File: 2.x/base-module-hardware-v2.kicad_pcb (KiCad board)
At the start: 4 copper layers, 100 x 99.7 mm, 271 parts, among them K1 CONN_3, P1 PINBALL-CONNECTOR, P2 PINBALL-CONNECTOR, P3 SOLENOID-CONNECTOR, P4 CONN_16, P5 CONN_16, P6 HE10-32, Q1 BC846, Q10 DMN6040SSD, Q11 BC846, Q12 BC846, Q13 DMP2240UDM, Q14 DMP2240UDM, Q15 BC846, Q16 BC846, Q17 BC846, Q18 BC846, Q19 DMN6040SSD, Q2 BC846, Q20 DMN6040SSD, Q21 BC846, Q22 BC846, Q23 BC846, Q24 BC846, Q25 BC846, Q26 BC846, Q27 BC846, Q28 BC846, Q29 BSS138, Q3 DMN6040SSD, Q30 FDD5614P, Q31 BC846, Q32 BSS138, Q4 DMN6040SSD, Q5 BC846, Q6 BC846, Q7 BC846, Q8 BC846, Q9 DMN6040SSD, U1 74LVC14, U2 STM32F072R, U3 MCP2562, U4 MC78L05ACH, U5 AP1117IE33G, U6 ZXCT1086E5TA, U7 ZXCT1107SA-7, U8 LM7805CT, U9 MMA8653FC, X1 8.000 MHz

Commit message: Tweaking layout to make power supply fit
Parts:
- moved SERIAL1 83.3 mm to (132.4, 53.0)
- moved C11 80.0 mm to (43.8, -22.9)
- moved U3 80.0 mm to (43.5, -17.8)
- moved C12 80.0 mm to (43.5, -12.7)
- moved ADR1 79.5 mm to (175.9, 100.6)
- moved R109 79.5 mm to (174.0, 106.4)
- moved R112 79.5 mm to (177.8, 109.5)
- moved R108 79.5 mm to (172.7, 109.5)
- moved R111 79.5 mm to (176.5, 106.4)
- moved R113 79.5 mm to (179.1, 106.4)
- moved R114 79.5 mm to (180.3, 109.5)
- moved R107 79.5 mm to (171.4, 106.4)
- moved R110 79.5 mm to (175.3, 109.5)
- moved Q29 75.2 mm to (84.1, -40.3)
- moved C16 75.0 mm to (57.8, -1.91)
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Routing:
- net /Control Logic/LAMP_ROW1: track 48.4 -> 0.00 mm, vias 2 -> 0
- net /Control Logic/LAMP_ROW0: track 45.1 -> 0.00 mm, vias 2 -> 0
- net /Control Logic/SOLENOID7: track 44.8 -> 0.00 mm, vias 2 -> 0
- net /Control Logic/SOLENOID6: track 41.5 -> 0.00 mm, vias 2 -> 0
- net /Control Logic/LAMP_ROW3: track 39.1 -> 0.00 mm, vias 2 -> 0
- net /Control Logic/SOLENOID5: track 37.9 -> 0.00 mm, vias 2 -> 0
- net /Control Logic/LAMP_ROW2: track 37.4 -> 0.00 mm, vias 2 -> 0
- net /Control Logic/SOLENOID4: track 35.5 -> 0.00 mm, vias 2 -> 0
- net GND: track 169.6 -> 202.6 mm, vias 53 -> 62
- net /Control Logic/SOLENOID3: track 32.1 -> 0.00 mm, vias 2 -> 0
- net /Control Logic/ADDRESS0: track 34.3 -> 5.06 mm, vias 2 -> 0
- net /Control Logic/ADDRESS7: track 30.3 -> 1.89 mm, vias 2 -> 0
- net /Control Logic/ADDRESS6: track 31.8 -> 5.06 mm, vias 2 -> 0
- net Net-(D18-Pad1): track 93.7 -> 67.1 mm
- net /Control Logic/SOLENOID2: track 26.1 -> 0.00 mm, vias 2 -> 0
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
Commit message: Everything fits on the board area now. Still need to finish wiring.
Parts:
- moved C11 144.7 mm to (84.8, 115.9), turned to 270 degrees
- moved R124 142.3 mm to (128.0, 153.0)
- moved R128 142.3 mm to (128.0, 147.0)
- moved U7 142.3 mm to (128.0, 149.9)
- moved U3 141.8 mm to (89.9, 116.2), turned to 180 degrees
- moved C12 138.8 mm to (94.9, 116.2), turned to 270 degrees
- moved R102 138.3 mm to (104.5, 115.9), turned to 180 degrees
- moved D35 138.2 mm to (70.8, 129.9)
- moved R130 138.0 mm to (67.9, 129.9)
- moved D36 137.6 mm to (70.8, 131.8)
- moved R131 137.1 mm to (67.9, 131.8)
- moved D37 136.8 mm to (70.8, 133.7)
- moved R132 136.3 mm to (67.9, 133.7)
- moved R119 136.2 mm to (101.9, 92.7)
- moved U6 136.2 mm to (105.4, 92.7)
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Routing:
- net /RGB LED Output/RGB_DATA: track 0.00 -> 90.8 mm, vias 0 -> 2
- net /Control Logic/BOOTLOADER: track 0.00 -> 69.6 mm, vias 0 -> 1
- net /Control Logic/LAMP_ROW1: track 0.00 -> 63.7 mm, vias 0 -> 2
- net /Control Logic/LAMP_ROW0: track 0.00 -> 63.5 mm, vias 0 -> 2
- net /Switch Matrix/ROW0: track 64.9 -> 3.71 mm
- net /Switch Matrix/ROW3: track 64.1 -> 4.29 mm, vias 2 -> 0
- net /Switch Matrix/ROW1: track 63.1 -> 3.57 mm
- net /Switch Matrix/ROW2: track 61.3 -> 2.02 mm
- net /Control Logic/SOLENOID7: track 0.00 -> 52.4 mm, vias 0 -> 2
- net /Control Logic/SOLENOID6: track 0.00 -> 47.6 mm, vias 0 -> 2
- net /Control Logic/SOLENOID5: track 0.00 -> 42.8 mm, vias 0 -> 2
- net /Control Logic/~RESET: track 0.00 -> 42.8 mm, vias 0 -> 1
- net /Control Logic/SOLENOID0: track 0.00 -> 42.4 mm, vias 0 -> 2
- net /Control Logic/LAMP_ROW2: track 0.00 -> 42.4 mm, vias 0 -> 2
- net /Control Logic/SOLENOID2: track 0.00 -> 41.0 mm, vias 0 -> 2
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
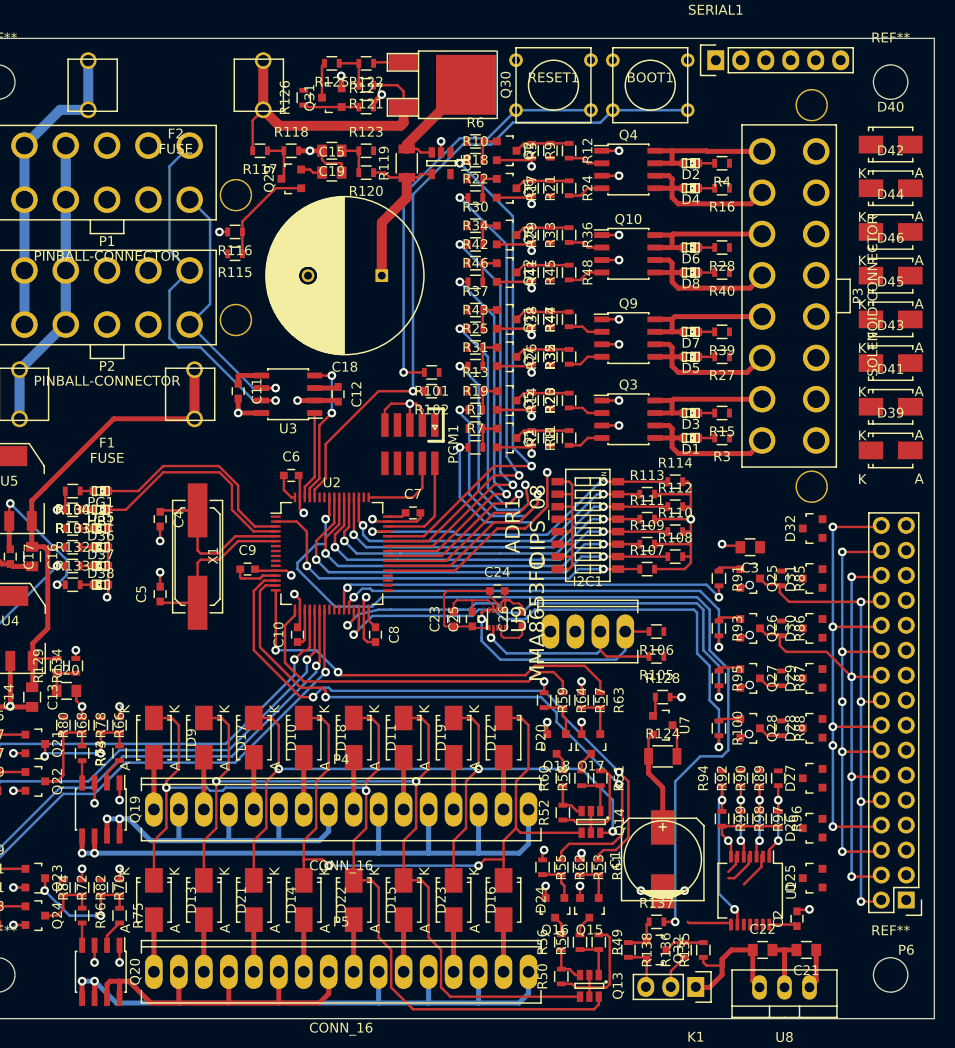
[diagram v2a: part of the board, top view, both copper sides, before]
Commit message: 2.0 is getting very close. Adjusted the solenoid connections to allow a cleaner layout.
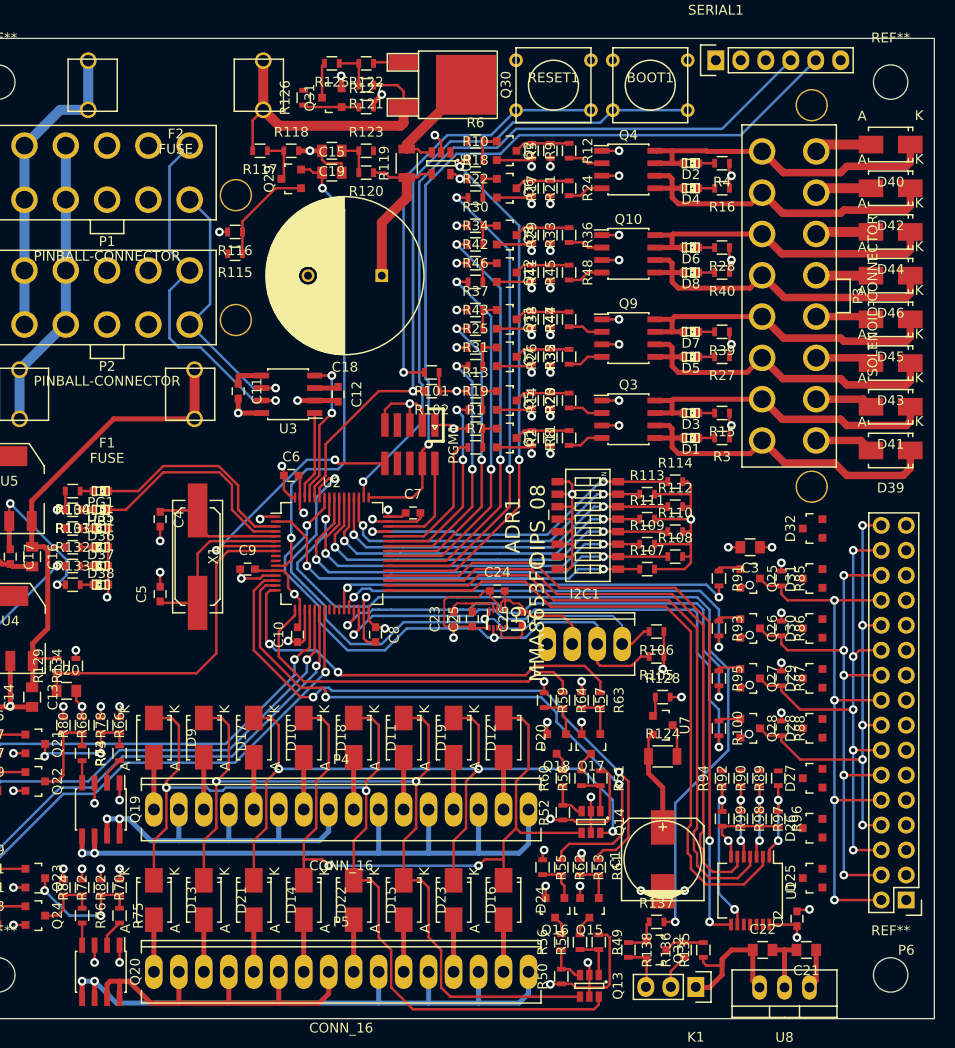
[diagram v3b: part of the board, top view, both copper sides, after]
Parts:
- moved I2C1 1.31 mm to (120.0, 141.6)
- turned D39 to 180 degrees
- turned D40 to 180 degrees
- turned D41 to 180 degrees
- turned D42 to 180 degrees
- turned D43 to 180 degrees
- turned D44 to 180 degrees
- turned D45 to 180 degrees
- turned D46 to 180 degrees
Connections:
- U2 pad 37: /Control Logic/SOLENOID0 -> /Control Logic/SOLENOID7
- U2 pad 38: /Control Logic/SOLENOID1 -> /Control Logic/SOLENOID6
- U2 pad 39: /Control Logic/SOLENOID2 -> /Control Logic/SOLENOID5
- U2 pad 40: /Control Logic/SOLENOID3 -> /Control Logic/SOLENOID4
- U2 pad 41: /Control Logic/SOLENOID4 -> /Control Logic/SOLENOID3
- U2 pad 42: /Control Logic/SOLENOID5 -> /Control Logic/SOLENOID2
- U2 pad 43: /Control Logic/SOLENOID6 -> /Control Logic/SOLENOID1
- U2 pad 44: /Control Logic/SOLENOID7 -> /Control Logic/SOLENOID0
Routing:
- net +12V: track 58.1 -> 154.4 mm, vias 0 -> 17
- net /Control Logic/RXD: track 0.00 -> 77.7 mm, vias 0 -> 1
- net /Control Logic/SWCLK: track 8.35 -> 82.0 mm, vias 0 -> 1
- net /Switch Matrix/ROW3: track 4.29 -> 68.5 mm, vias 0 -> 2
- net /Switch Matrix/ROW0: track 3.71 -> 67.6 mm
- net /Switch Matrix/ROW2: track 2.02 -> 64.4 mm
- net /Switch Matrix/ROW1: track 3.57 -> 65.9 mm
- net +3.3V: track 73.8 -> 130.7 mm, vias 2 -> 19
- net /Control Logic/VSOL_IN_SENSE: track 2.33 -> 48.6 mm, vias 0 -> 2
- net /Solenoid Driver/SOL_PWR: track 17.3 -> 63.5 mm
- net /Accelerometer/SDA: track 23.9 -> 60.4 mm, vias 1 -> 2
- net /Accelerometer/SCL: track 22.0 -> 58.0 mm, vias 1 -> 2
- net /Control Logic/12V_SENSE: track 3.71 -> 34.6 mm
- net /Control Logic/~RESET: track 42.8 -> 71.1 mm, vias 1 -> 3
- net /Control Logic/SOLENOID0: track 42.4 -> 15.1 mm, vias 2 -> 0
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
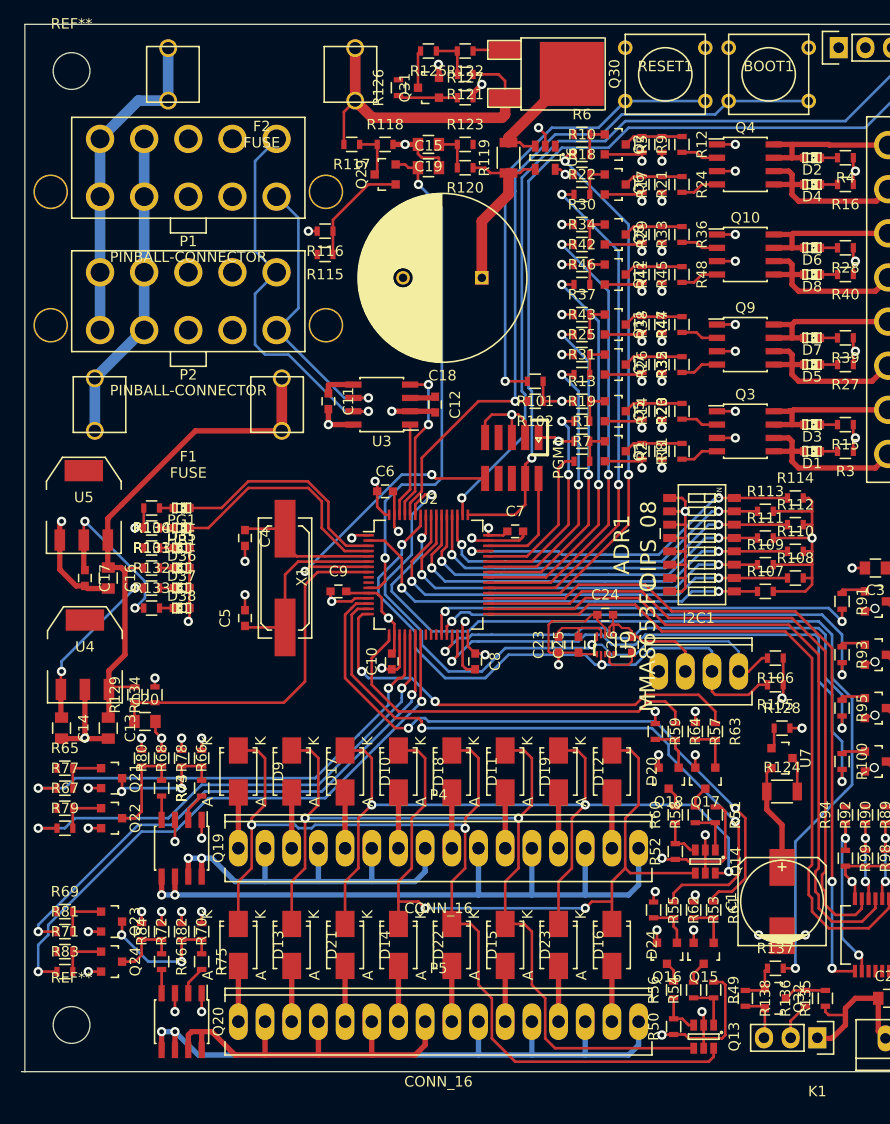
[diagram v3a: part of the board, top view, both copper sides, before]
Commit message: Power layers set up. A few footprint/pinout changes and some silkscreen cleanup, and the first rev is complete.
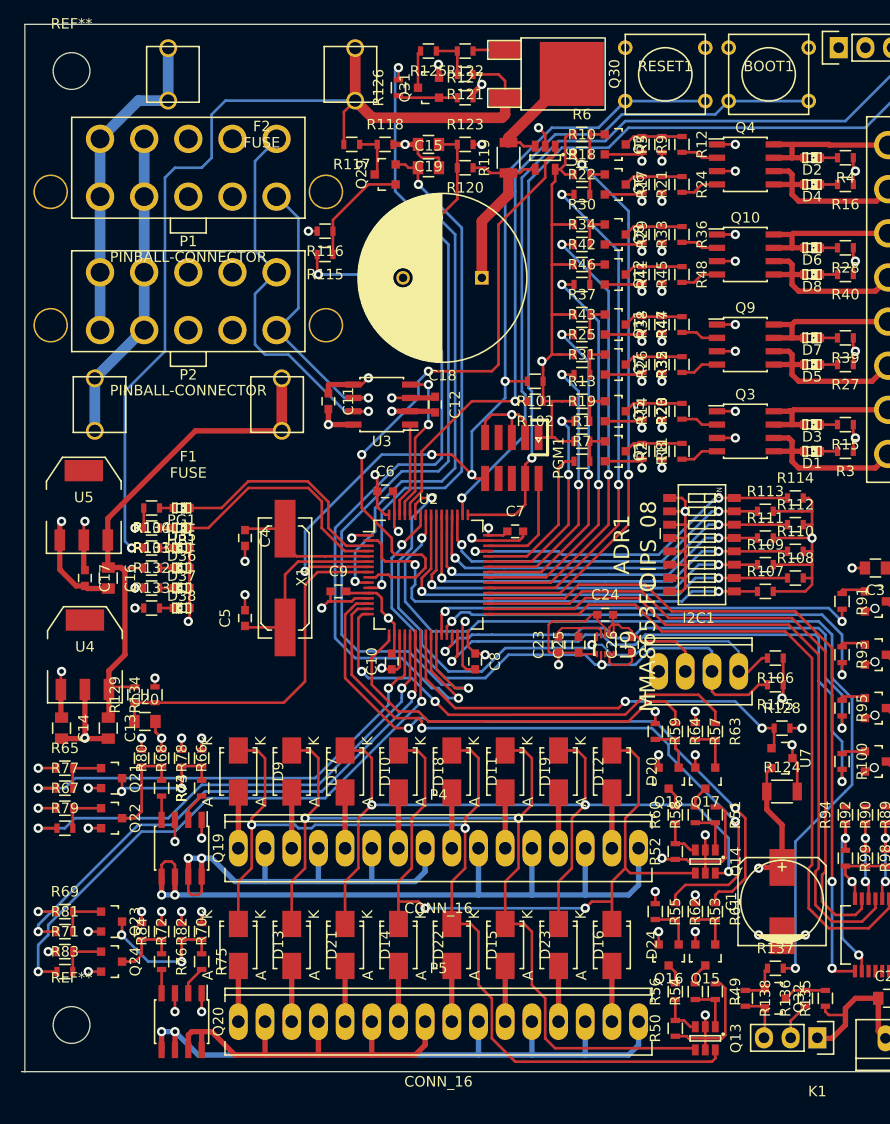
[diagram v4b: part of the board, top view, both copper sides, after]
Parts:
- moved Q13 0.22 mm to (120.7, 176.5)
- moved Q15 0.22 mm to (120.7, 168.6)
- moved R49 0.22 mm to (121.6, 172.1)
- moved R53 0.22 mm to (119.7, 164.5)
- moved R54 0.22 mm to (119.7, 172.1)
- moved R61 0.22 mm to (121.6, 164.5)
- moved Q16 0.22 mm to (117.2, 168.6)
- moved R50 0.22 mm to (117.8, 175.6)
- moved R55 0.22 mm to (115.9, 164.5)
- moved R56 0.22 mm to (117.8, 172.1)
- moved R62 0.22 mm to (117.8, 164.5)
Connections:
- U2 pad 10: /Power Supply/ILAMP_SENSE_OUT -> /Control Logic/VSOL_SENSE
- U2 pad 24: /Control Logic/VSOL_SENSE -> /Power Supply/ILAMP_SENSE_OUT
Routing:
- net /Control Logic/VSOL_PRECHARGE_PWM: track 0.00 -> 84.9 mm, vias 0 -> 2
- net +3.3V: track 130.7 -> 204.1 mm, vias 19 -> 18
- net /Control Logic/VSOL_MEASURE_CONTROL: track 0.00 -> 71.5 mm, vias 0 -> 2
- net VEE: track 31.2 -> 93.0 mm, vias 0 -> 1
- net /Power Supply/ISOL_SENSE_OUT: track 0.00 -> 61.5 mm, vias 0 -> 2
- net /Control Logic/VSOL_SENSE: track 3.97 -> 52.2 mm, vias 0 -> 2
- net +5V: track 19.7 -> 66.0 mm, vias 2 -> 3
- net /Power Supply/ILAMP_SENSE_OUT: track 2.01 -> 41.8 mm, vias 0 -> 2
- net /Control Logic/~RESET: track 71.1 -> 85.1 mm, vias 3 -> 4
- net Net-(P4-Pad2): track 39.1 -> 43.5 mm
- net Net-(P4-Pad10): track 66.1 -> 69.9 mm
- net /Control Logic/VSOL_IN_SENSE: track 48.6 -> 50.5 mm
- net /Accelerometer/SDA: track 60.4 -> 58.9 mm
- net /Control Logic/ADDRESS7: track 41.5 -> 42.9 mm
- net +12V: track 154.4 -> 155.7 mm, vias 17 -> 18
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- added copper zone on Power.Cu, net +12V
- added copper zone on Power.Cu, net +3.3V
- added copper zone on Power.Cu, net /Lamp Driver/LAMP_12V
- added copper zone on Power.Cu, net /Solenoid Driver/SOL_PWR

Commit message: 100% routed.
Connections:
- D25 pad 2: /Switch Matrix/ROW0_SWITCHED -> Net-(D25-Pad2)
- D25 pad 3: Net-(D25-Pad3) -> /Switch Matrix/ROW0_SWITCHED
- D26 pad 2: /Switch Matrix/ROW0_SWITCHED -> Net-(D26-Pad2)
- D26 pad 3: Net-(D26-Pad3) -> /Switch Matrix/ROW0_SWITCHED
- D27 pad 2: /Switch Matrix/ROW1_SWITCHED -> Net-(D27-Pad2)
- D27 pad 3: Net-(D27-Pad3) -> /Switch Matrix/ROW1_SWITCHED
- D28 pad 2: /Switch Matrix/ROW1_SWITCHED -> Net-(D28-Pad2)
- D28 pad 3: Net-(D28-Pad3) -> /Switch Matrix/ROW1_SWITCHED
- D29 pad 2: /Switch Matrix/ROW2_SWITCHED -> Net-(D29-Pad2)
- D29 pad 3: Net-(D29-Pad3) -> /Switch Matrix/ROW2_SWITCHED
- D30 pad 2: /Switch Matrix/ROW2_SWITCHED -> Net-(D30-Pad2)
- D30 pad 3: Net-(D30-Pad3) -> /Switch Matrix/ROW2_SWITCHED
- D31 pad 2: /Switch Matrix/ROW3_SWITCHED -> Net-(D31-Pad2)
- D31 pad 3: Net-(D31-Pad3) -> /Switch Matrix/ROW3_SWITCHED
- D32 pad 2: /Switch Matrix/ROW3_SWITCHED -> Net-(D32-Pad2)
- D32 pad 3: Net-(D32-Pad3) -> /Switch Matrix/ROW3_SWITCHED
- P6 pad 11: Net-(D27-Pad3) -> Net-(D27-Pad2)
- P6 pad 15: Net-(D28-Pad3) -> Net-(D28-Pad2)
- P6 pad 19: Net-(D29-Pad3) -> Net-(D29-Pad2)
- P6 pad 23: Net-(D30-Pad3) -> Net-(D30-Pad2)
- P6 pad 27: Net-(D31-Pad3) -> Net-(D31-Pad2)
- P6 pad 3: Net-(D25-Pad3) -> Net-(D25-Pad2)
- P6 pad 31: Net-(D32-Pad3) -> Net-(D32-Pad2)
- P6 pad 7: Net-(D26-Pad3) -> Net-(D26-Pad2)
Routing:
- net /Switch Matrix/ROW3_SWITCHED: track 0.00 -> 31.1 mm, vias 0 -> 3
- net /Switch Matrix/ROW2_SWITCHED: track 0.00 -> 20.3 mm, vias 0 -> 3
- net /Switch Matrix/ROW0_SWITCHED: track 0.00 -> 12.4 mm
- net /Switch Matrix/ROW1_SWITCHED: track 0.00 -> 10.5 mm, vias 0 -> 2
- net Net-(D27-Pad2): track 0.00 -> 9.58 mm
- net Net-(D31-Pad2): track 0.00 -> 9.31 mm
- net Net-(D29-Pad2): track 0.00 -> 9.31 mm
- net Net-(D26-Pad2): track 0.00 -> 9.31 mm
- net Net-(D28-Pad2): track 0.00 -> 9.31 mm
- net Net-(D32-Pad2): track 0.00 -> 9.31 mm
- net Net-(D30-Pad2): track 0.00 -> 9.31 mm
- net Net-(D25-Pad2): track 0.00 -> 9.31 mm
- net Net-(D32-Pad1): track 0.00 -> 9.05 mm
- net Net-(D31-Pad1): track 0.00 -> 9.05 mm
- net Net-(D30-Pad1): track 0.00 -> 9.05 mm
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
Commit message: Finished layout! Needs review.
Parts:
- added G***: DIYPINBALL-LOGO-SMALL, PinballParts:diypinball-logo-small, F.Cu at (109.2, 129.9)
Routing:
- net /Switch Matrix/COL2: track 50.7 -> 50.0 mm
- net /Accelerometer/SDA: track 58.9 -> 58.1 mm
- net /Switch Matrix/COL3: track 55.4 -> 54.6 mm
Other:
- board size 100 x 99.7 mm -> 99.7 x 99.7 mm
- board text added: "DIYPinball Base Board Version 2.0"

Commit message: Added OSHW logo
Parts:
- added FIDUCIAL: VAL**, PinballParts:FIDUCIAL, F.Cu at (146.7, 87.3)
- added FIDUCIAL: VAL**, PinballParts:FIDUCIAL, F.Cu at (65.4, 173.7)
- added REF**: Symbol_OSHW-Logo_SilkScreen, Symbols:Symbol_OSHW-Logo_SilkScreen, B.Cu at (120.7, 174.3)
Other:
- board text added: "12V"
- board text added: "3.3V"
- board text added: "5V"
- board text added: "VSOL"
